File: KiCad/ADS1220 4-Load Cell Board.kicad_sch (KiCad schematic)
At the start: 20 parts, among them J1 Conn_01x04, J2 Conn_01x04, J3 Conn_01x04, J7 Conn_01x04

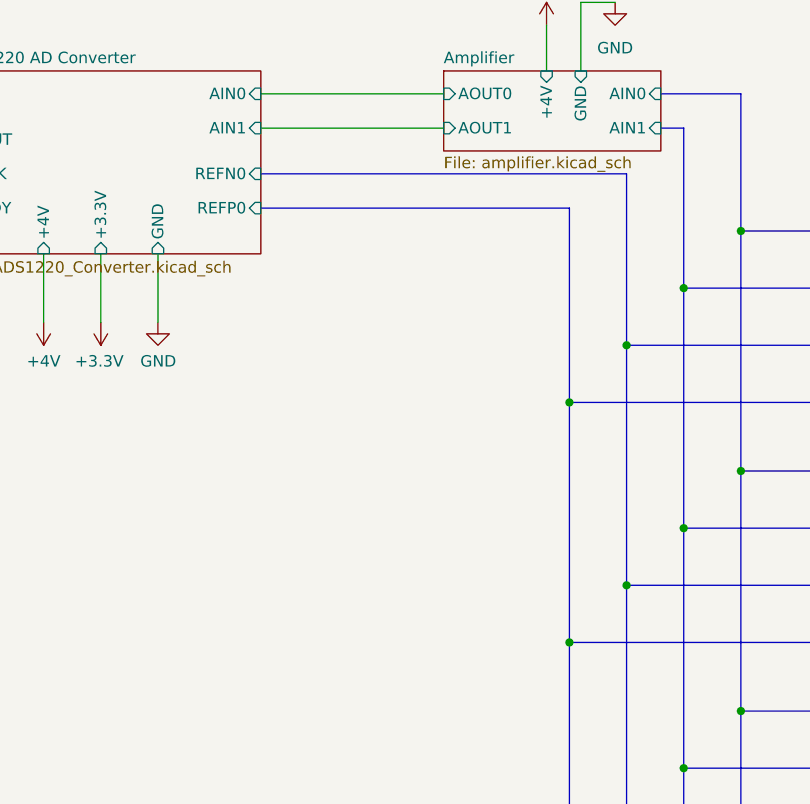
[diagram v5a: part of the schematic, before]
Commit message: Add Single Wire Debug
* Add Single Wire Debug (SWD) Tag Connect Connector
* Re-layout of 5V power so the 5V pins connect to a pad directly behind the USB connector
* Add 0R resistors to air gap the 3.3V and 5V power rails for incremental board bringup
* Rotate ADS1220 for cleaner layout
* Remove connections to reference voltage pins, since AVDD/AVSS is a valid reference

fixup

fixup

fixup
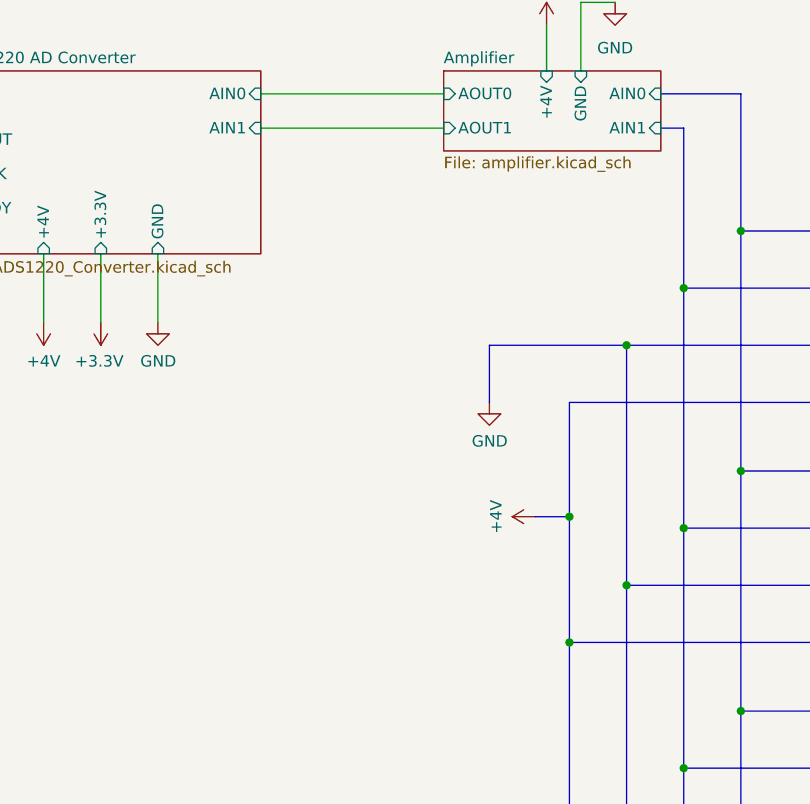
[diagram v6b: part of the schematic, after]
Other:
- sheet ADS1220 AD Converter ports: added none; removed REFN0, REFP0
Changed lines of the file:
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@@
 	(paper "A4")
 	(junction
-		(at 193.04 63.5)
+		(at 186.69 82.55)
 		(diameter 0)
 		(color 0 0 0 0)
 	)
 	(junction
-		(at 193.04 116.84)
+		(at 193.04 63.5)
 		(diameter 0)
 		(color 0 0 0 0)
 	)
 	(junction
-		(at 57.15 93.98)
+		(at 193.04 116.84)
 		(diameter 0)
 		(color 0 0 0 0)
 	)
 	(junction
-		(at 186.69 69.85)
+		(at 57.15 93.98)
 		(diameter 0)
 		(color 0 0 0 0)
@@
 		)
 	)
+	(bus
+		(pts
+			(xy 177.8 63.5) (xy 193.04 63.5)
+		)
+		(stroke
+			(width 0)
+			(type default)
+		)
+	)
 	(wire
 		(pts
@@
 		)
 	)
-	(bus
-		(pts
-			(xy 152.4 48.26) (xy 186.69 48.26)
-		)
-		(stroke
-			(width 0)
-			(type default)
-		)
-	)
 	(wire
 		(pts
@@
 	(bus
 		(pts
-			(xy 186.69 69.85) (xy 186.69 96.52)
+			(xy 186.69 69.85) (xy 186.69 82.55)
 		)
 		(stroke
@@
 		)
 	)
-	(bus
-		(pts
-			(xy 186.69 48.26) (xy 186.69 69.85)
-		)
-		(stroke
-			(width 0)
-			(type default)
-		)
-	)
 	(wire
 		(pts
@@
 	(bus
 		(pts
-			(xy 193.04 44.45) (xy 193.04 63.5)
+			(xy 186.69 82.55) (xy 186.69 96.52)
 		)
 		(stroke
@@
 	(bus
 		(pts
+			(xy 182.88 82.55) (xy 186.69 82.55)
+		)
+		(stroke
+			(width 0)
+			(type default)
+		)
+	)
+	(bus
+		(pts
 			(xy 205.74 77.47) (xy 205.74 104.14)
 		)
@@
 	(bus
 		(pts
-			(xy 152.4 44.45) (xy 193.04 44.45)
-		)
-		(stroke
-			(width 0)
-			(type default)
-		)
-	)
-	(bus
-		(pts
 			(xy 193.04 116.84) (xy 193.04 143.51)
 		)
@@
 	(bus
 		(pts
+			(xy 177.8 69.85) (xy 177.8 63.5)
+		)
+		(stroke
+			(width 0)
+			(type default)
+		)
+	)
+	(bus
+		(pts
 			(xy 186.69 96.52) (xy 186.69 123.19)
 		)
@@
 	)
 	(symbol
+		(lib_id "power:GND")
+		(at 177.8 69.85 0)
+		(unit 1)
+		(exclude_from_sim no)
+		(in_bom yes)
+		(on_board yes)
+		(dnp no)
+		(property "Reference" "#PWR045"
+			(at 177.8 76.2 0)
+			(effects
+				(font
+					(size 1.27 1.27)
+				)
+				(hide yes)
+			)
+		)
+		(property "Value" "GND"
+			(at 179.832 74.168 0)
+			(effects
+				(font
+					(size 1.27 1.27)
+				)
+				(justify right)
+			)
+		)
+		(property "Footprint" ""
+			(at 177.8 69.85 0)
+			(effects
+				(font
+					(size 1.27 1.27)
+				)
+				(hide yes)
+			)
+		)
+		(property "Datasheet" ""
+			(at 177.8 69.85 0)
+			(effects
+				(font
+					(size 1.27 1.27)
+				)
+				(hide yes)
+			)
+		)
+		(property "Description" "Power symbol creates a global label with name \"GND\" , ground"
+			(at 177.8 69.85 0)
+			(effects
+				(font
+					(size 1.27 1.27)
+				)
+				(hide yes)
+			)
+		)
+		(pin "1"
+		)
+		(instances
+			(project "ADS1220 4-Load Cell Board"
+				(path "/5d164854-6659-4076-ba4e-df0771b4723d"
+					(reference "#PWR045")
+					(unit 1)
+				)
+			)
+		)
+	)
+	(symbol
 		(lib_id "power:+4V")
 		(at 184.15 27.94 0)
@@
 	)
 	(symbol
+		(lib_id "power:+4V")
+		(at 182.88 82.55 90)
+		(unit 1)
+		(exclude_from_sim no)
+		(in_bom yes)
+		(on_board yes)
+		(dnp no)
+		(property "Reference" "#PWR036"
+			(at 186.69 82.55 0)
+			(effects
+				(font
+					(size 1.27 1.27)
+				)
+				(hide yes)
+			)
+		)
+		(property "Value" "+4V"
+			(at 178.562 82.55 0)
+			(effects
+				(font
+					(size 1.27 1.27)
+				)
+			)
+		)
+		(property "Footprint" ""
+			(at 182.88 82.55 0)
+			(effects
+				(font
+					(size 1.27 1.27)
+				)
+				(hide yes)
+			)
+		)
+		(property "Datasheet" ""
+			(at 182.88 82.55 0)
+			(effects
+				(font
+					(size 1.27 1.27)
+				)
+				(hide yes)
+			)
+		)
+		(property "Description" "Power symbol creates a global label with name \"+4V\""
+			(at 182.88 82.55 0)
+			(effects
+				(font
+					(size 1.27 1.27)
+				)
+				(hide yes)
+			)
+		)
+		(pin "1"
+		)
+		(instances
+			(project "ADS1220 4-Load Cell Board"
+				(path "/5d164854-6659-4076-ba4e-df0771b4723d"
+					(reference "#PWR036")
+					(unit 1)
+				)
+			)
+		)
+	)
+	(symbol
 		(lib_id "power:+3.3V")
 		(at 134.62 60.96 180)
@@
 			)
 		)
-		(pin "REFN0" input
-			(at 152.4 44.45 0)
-			(effects
-				(font
-					(size 1.27 1.27)
-				)
-				(justify right)
-			)
-		)
-		(pin "REFP0" input
-			(at 152.4 48.26 0)
-			(effects
-				(font
-					(size 1.27 1.27)
-				)
-				(justify right)
-			)
-		)

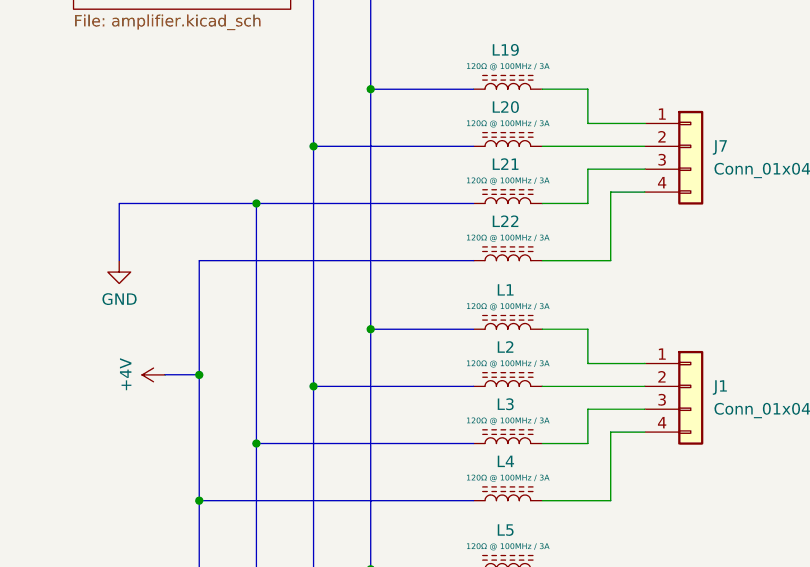
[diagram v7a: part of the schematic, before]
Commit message: Crystal Changes
* Update crystal selection, schematic and footprint
* Add resistor to limit drive current to crystal
* Block ground plane fill under crystal circuit
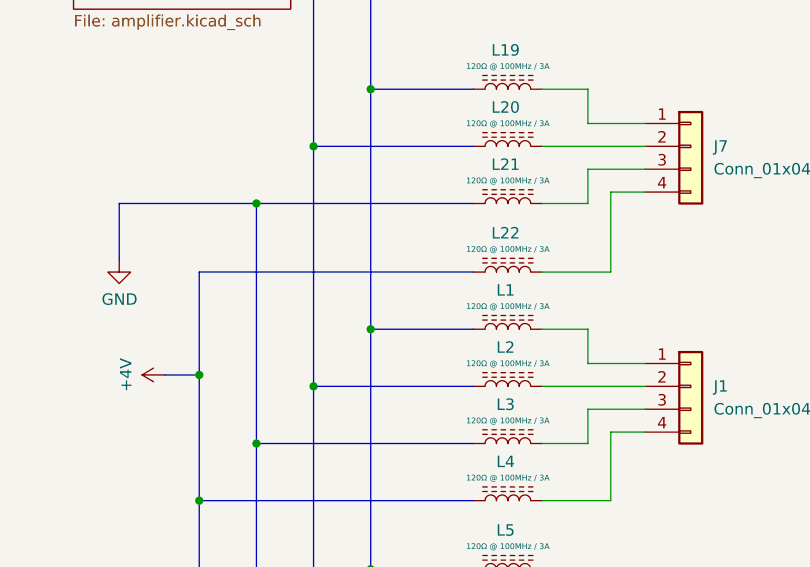
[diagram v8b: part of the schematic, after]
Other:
- moved on the sheet: L22
